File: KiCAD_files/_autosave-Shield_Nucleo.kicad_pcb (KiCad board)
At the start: 2 copper layers, 90 x 100 mm, 54 parts, among them J1 Shield_nucleo_stage_outline, J2 RJ45, J3 RJ45, U1 NUCLEO-F401RE, U2 AT25xxx, U3 TCAN334

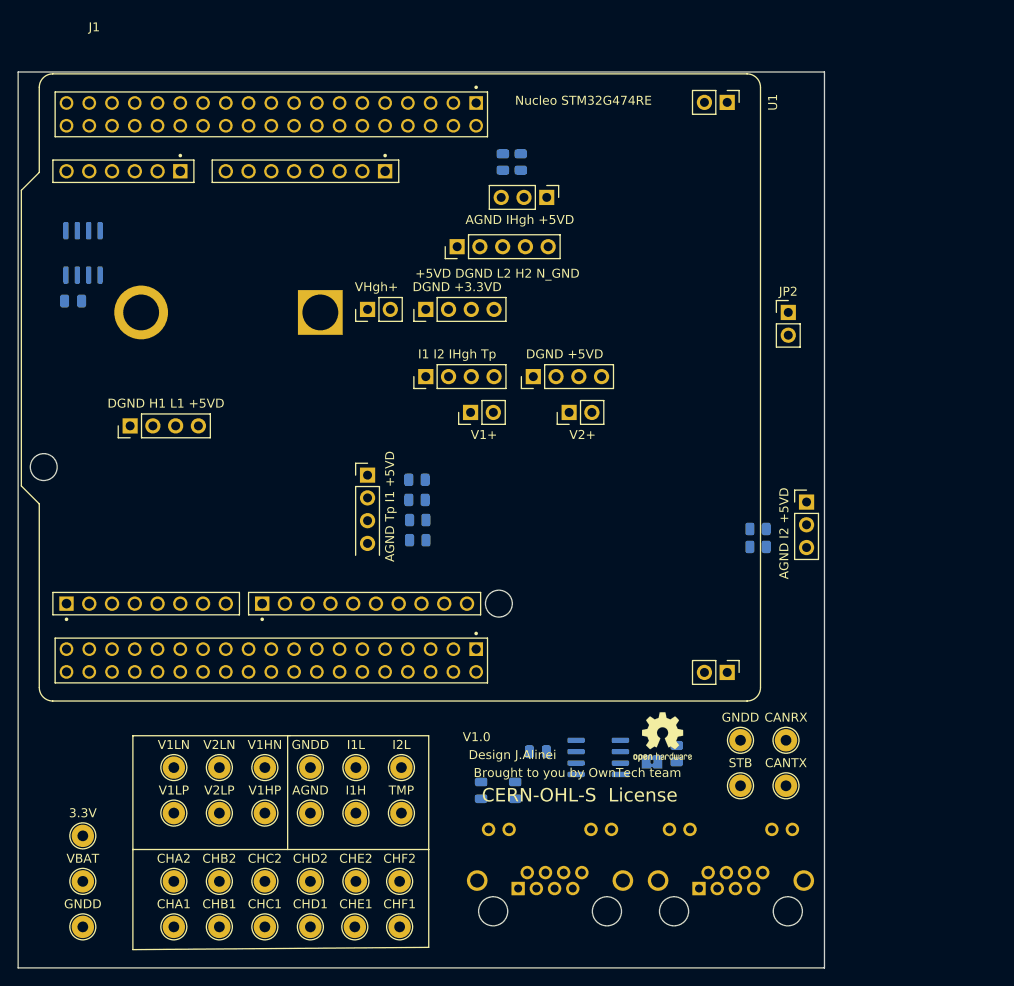
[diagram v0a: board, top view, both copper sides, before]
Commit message: Added remarks from Luiz revision
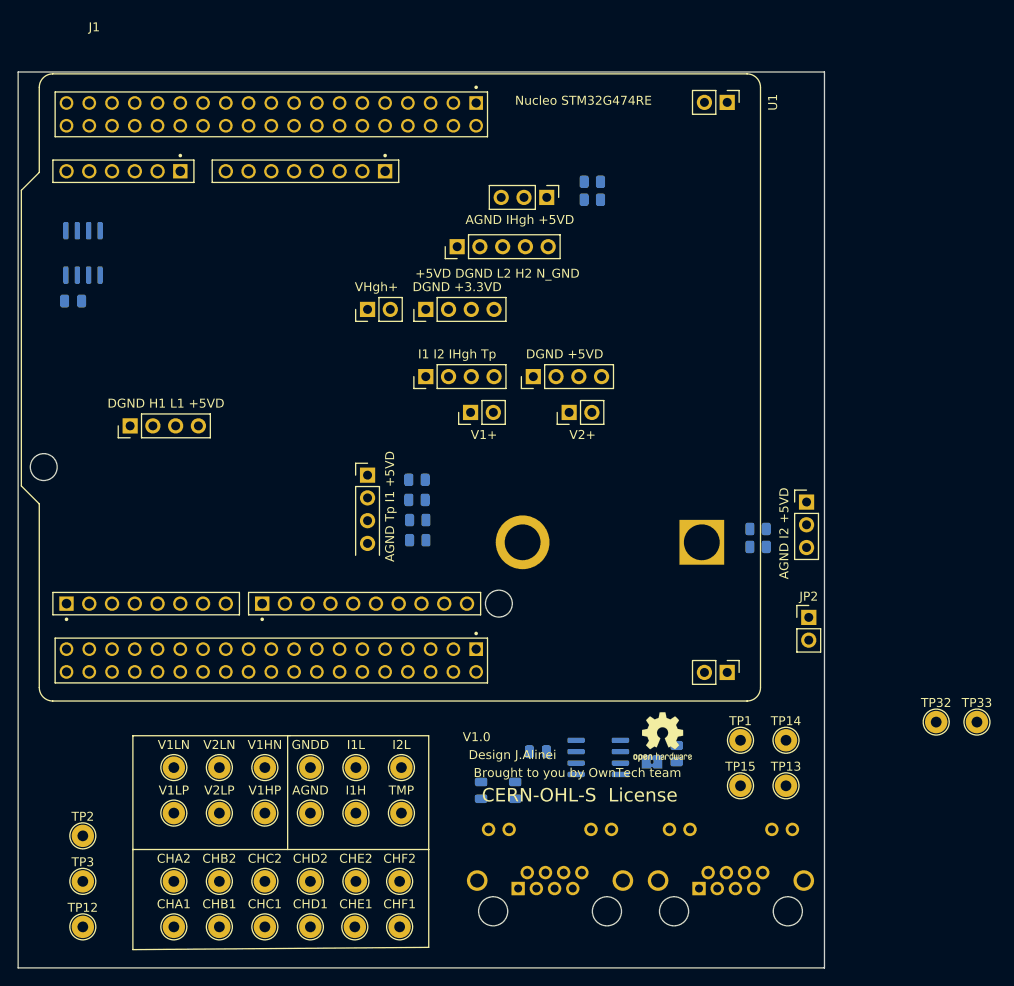
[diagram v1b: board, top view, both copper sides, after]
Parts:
- added TP32: TestPoint, TestPoint:TestPoint_THTPad_D2.5mm_Drill1.2mm, F.Cu at (141.0, 99.1)
- added TP33: TestPoint, TestPoint:TestPoint_THTPad_D2.5mm_Drill1.2mm, F.Cu at (145.5, 99.1)
- moved BT1 49.7 mm to (104.8, 79.0)
- moved JP2 34.1 mm to (126.7, 87.4)
- moved R7 10.8 mm to (102.6, 40.8), turned to 0 degrees
- moved R6 8.29 mm to (102.6, 38.8), turned to 180 degrees
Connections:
- net Net-(U1-PadCN7_17) renamed /HRTIM1_FLT2
- net Net-(U1-PadCN7_34) renamed /ADC3_XTRA
- U1 pad CN10_24: Net-(U1-PadCN10_24) -> /Temp
- U1 pad CN10_34: /Temp -> /ADC4_XTRA
- U1 pad CN7_2: /HRTIM_EEV2 -> /HRTIM_EEV1
- U1 pad CN7_3: /HRTIM_EEV1 -> /HRTIM_EEV2
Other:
- board text removed: "3.3V"
- board text removed: "CANRX"
- board text removed: "CANTX"
- board text removed: "STB"
- board text removed: "VBAT"
